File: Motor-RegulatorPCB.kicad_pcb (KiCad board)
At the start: 2 copper layers, 24.5 x 8.2 mm, 16 parts, among them U1 MIC3490-5.0YM5-TR

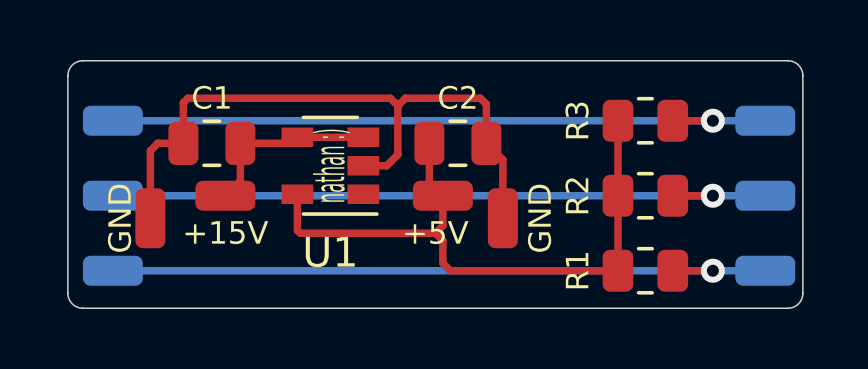
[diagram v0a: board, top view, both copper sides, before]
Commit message: moved 15V and 5V pads
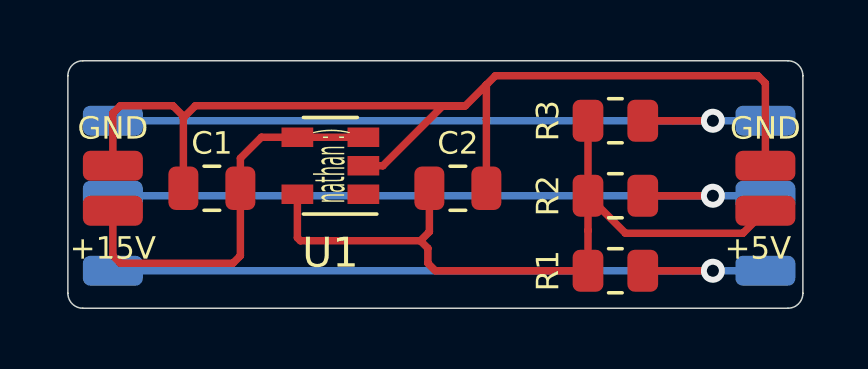
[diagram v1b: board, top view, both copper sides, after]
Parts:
- moved TP6 10.8 mm to (128.5, 82.0)
- moved TP10 8.92 mm to (128.5, 80.5), turned to 270 degrees
- moved TP1 3.78 mm to (106.8, 82.0), turned to 270 degrees
- moved TP5 2.15 mm to (106.8, 80.5), turned to 270 degrees
- moved C1 1.50 mm to (110.0, 81.2)
- moved C2 1.50 mm to (118.2, 81.2)
- moved R1 1.00 mm to (123.5, 84.0)
- moved R2 1.00 mm to (123.5, 81.5)
- moved R3 1.00 mm to (123.5, 79.0)
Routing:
- net GND: track 22.2 -> 37.3 mm
- net +15V: track 6.14 -> 13.6 mm
- net +5V: track 21.2 -> 25.5 mm
- net /HallC: track 23.1 -> 24.1 mm
- net /HallB: track 23.1 -> 24.1 mm
- net /HallA: track 23.1 -> 24.1 mm
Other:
- board text removed: "UTSVT - Motor Motor Regulator v1.0 Spring 2022"
